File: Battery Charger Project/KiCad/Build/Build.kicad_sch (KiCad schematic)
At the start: 26 parts, among them J1 Screw_Terminal_01x03, J2 Screw_Terminal_01x02, J3 Screw_Terminal_01x03, J4 726386-2, J5 726386-2, J6 726386-2, U1 LAUNCHXL-F28379D, U2 TMCS1133C3A

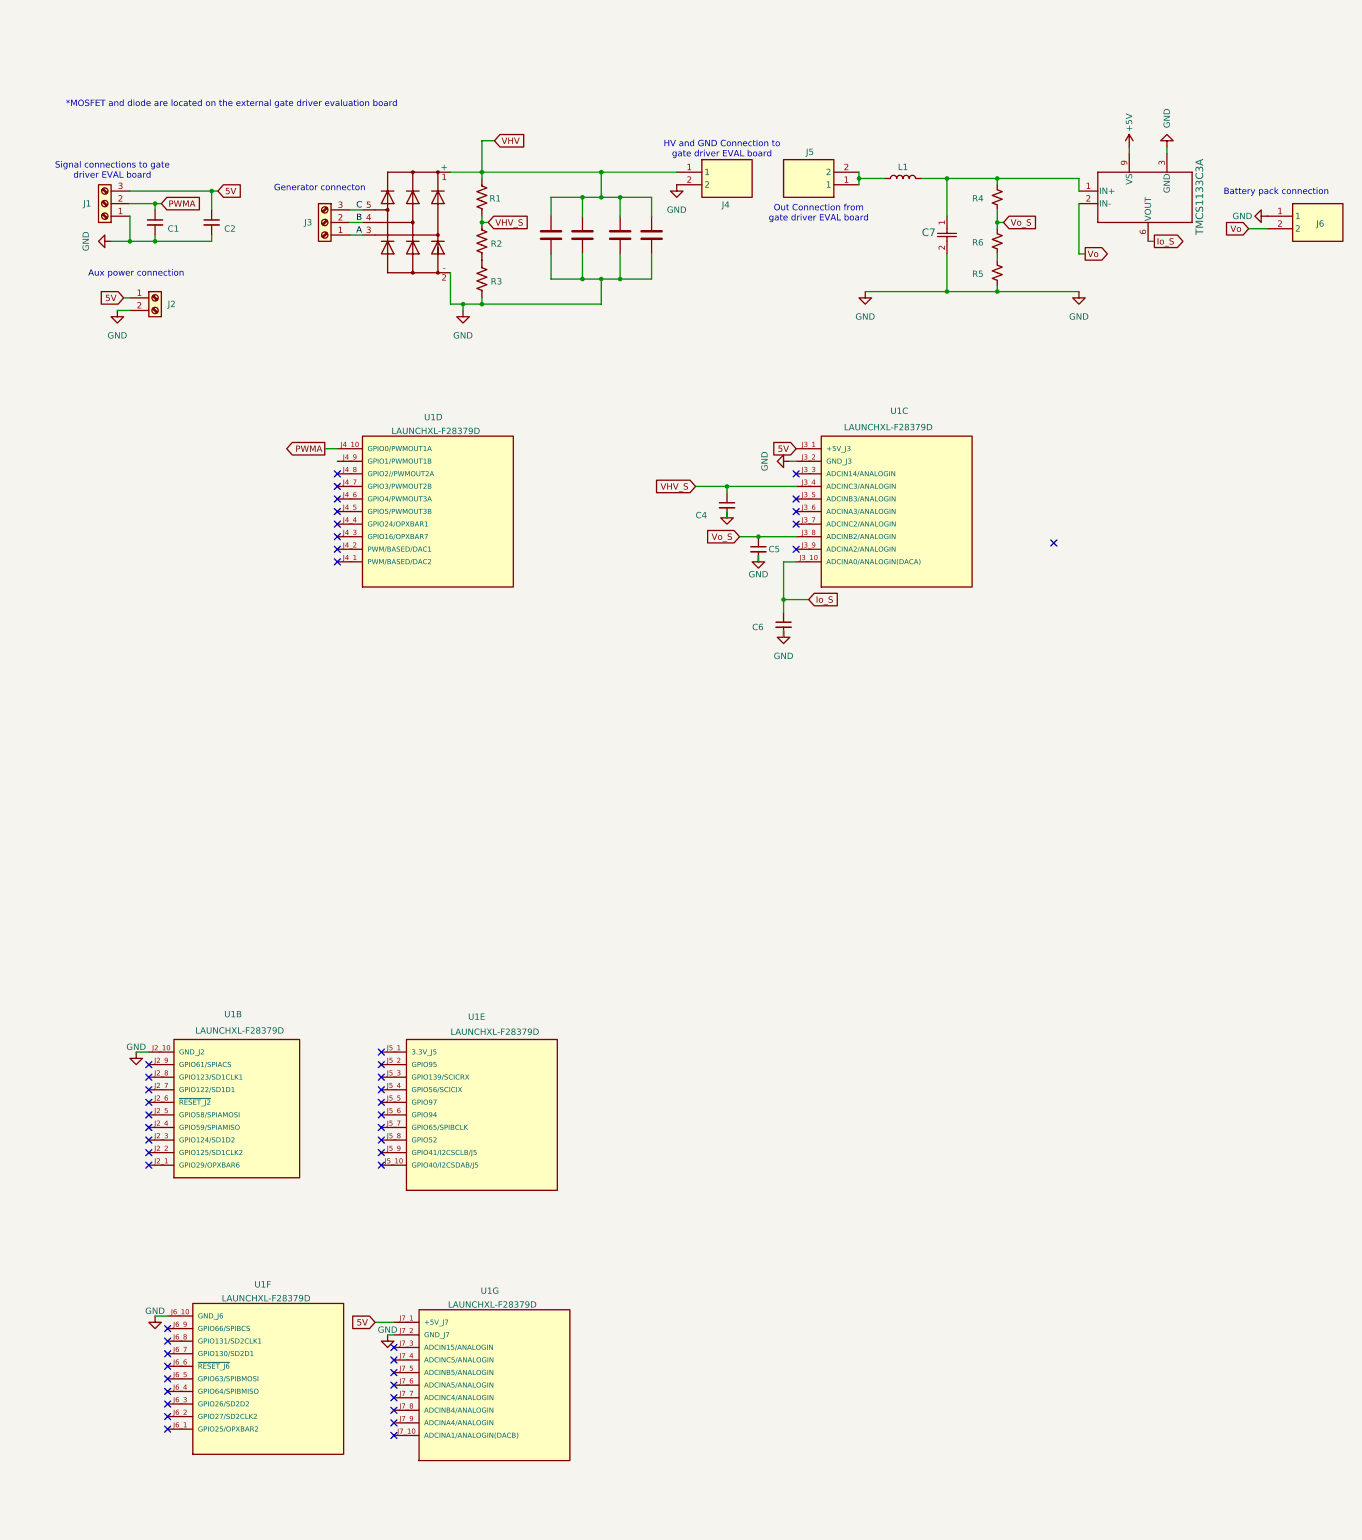
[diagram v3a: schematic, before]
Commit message: PCB updates
Dr. Mcintyre suggested using large pours for the high voltage and gnd planes. He also asked me to implement design constraints. The main concern is the distance between the high DC bus and gnd near the rectifier.
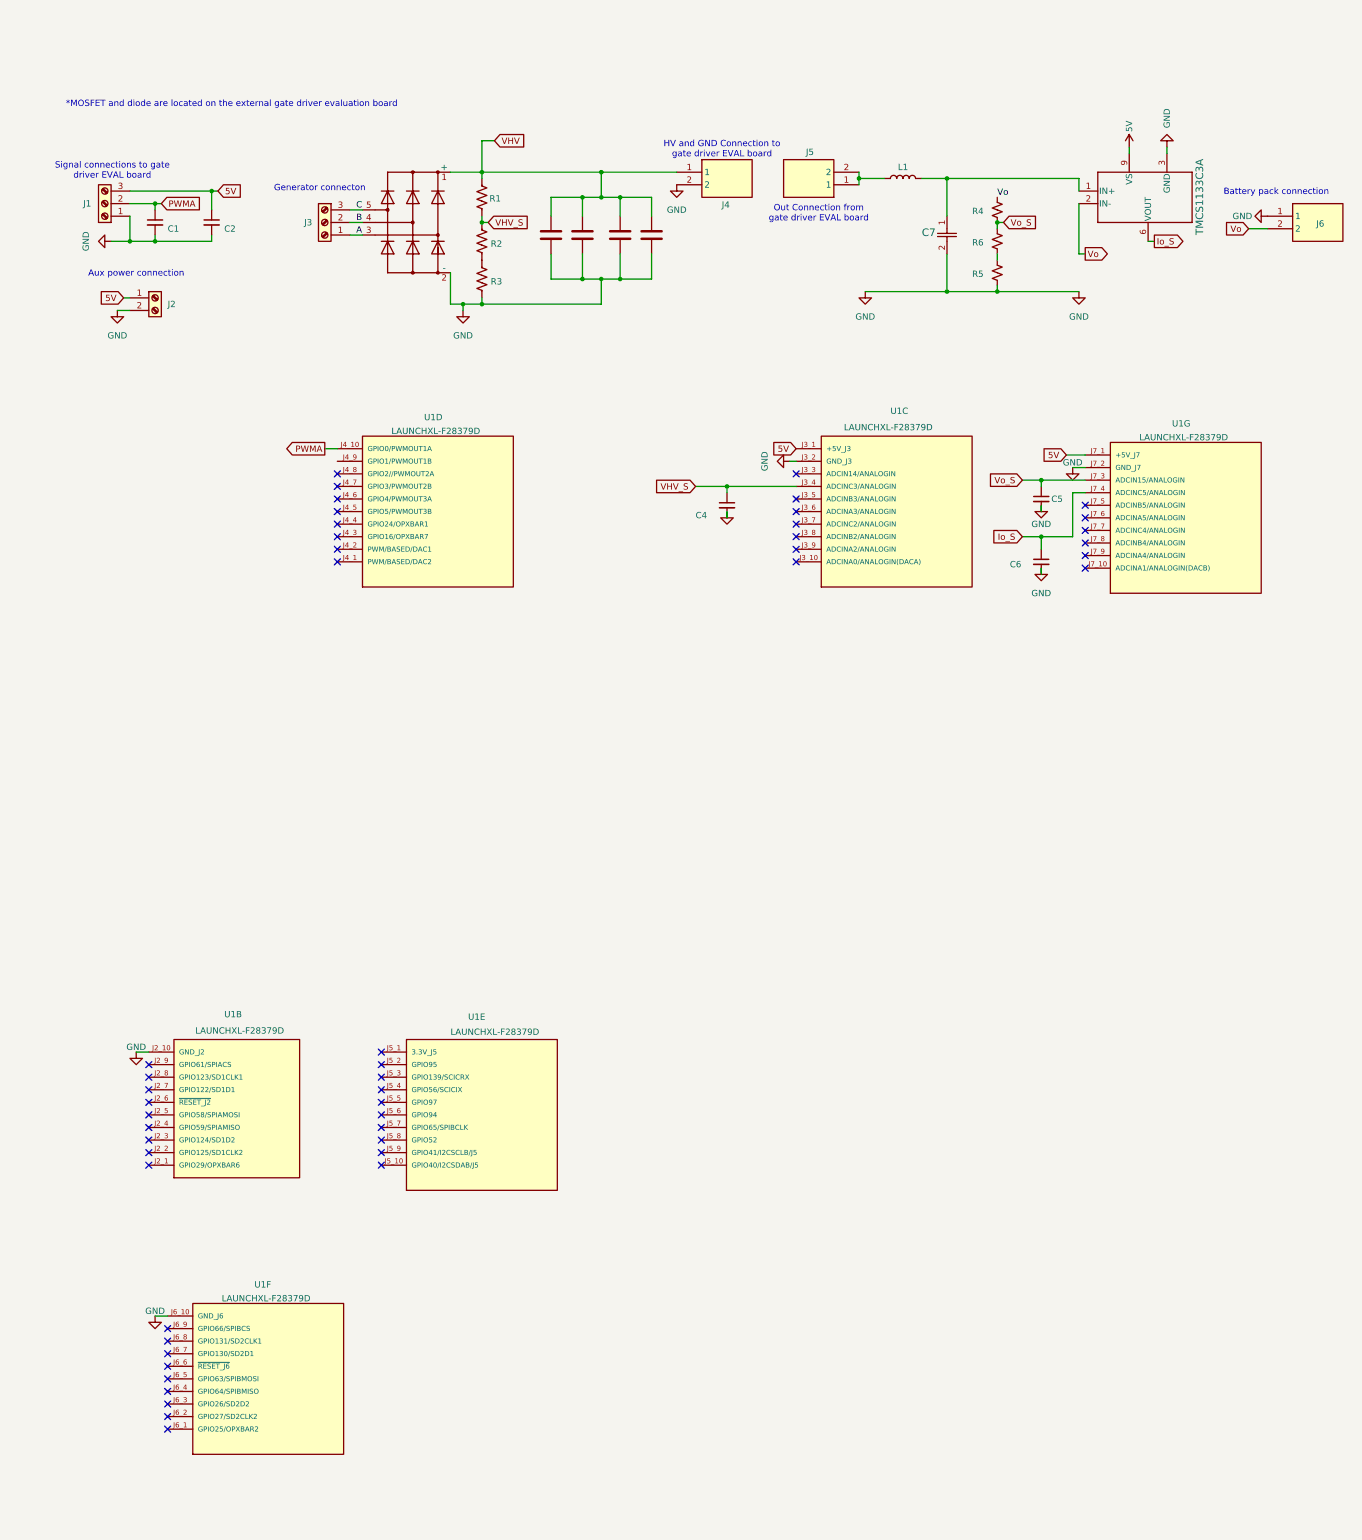
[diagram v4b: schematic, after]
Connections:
- net +5V is gone; now on net 5V: U2.9 (VS)
- net Io_S: now also U1.J7_4 (ADCINC5/ANALOGIN); no longer U1.J3_10 (ADCINA0/ANALOGIN(DACA))
- net Vo: now also R4.1
- net Vo_S: now also U1.J7_3 (ADCIN15/ANALOGIN); no longer U1.J3_8 (ADCINB2/ANALOGIN)
- net at C7.1, L1.2, U2.1 (IN+): no longer R4.1
- no-connect marks 50 -> 49
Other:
- moved on the sheet: C5, C6, R4, U1G

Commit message: PCB updates
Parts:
- added C11: C_Small, Capacitor_SMD:C_0805_2012Metric_Pad1.18x1.45mm_HandSolder, symbol Device:C_Small
- added unit 1 of U1
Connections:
- net 5V: no longer U1.J7_1 (+5V_J7), U2.9 (VS)
- net GND: now also C11.2
- net VHV_S: now also U1.J3_10 (ADCINA0/ANALOGIN(DACA)); no longer U1.J3_4 (ADCINC3/ANALOGIN)
- new net +3.3V: C11.1, U1.J1_1 (3.3V_J1), U2.10 (VS), U2.9 (VS)
- no-connect marks 49 -> 58
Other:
- moved on the sheet: C4, C5, C6, U1C, U1G

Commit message: PCB about done
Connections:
- net +3.3V: now also U2.8 (VOC)
- net GND: now also U2.4 (ALERT), U2.7 (OC)
- net Io_S: now also U1.J7_5 (ADCINB5/ANALOGIN); no longer U1.J7_4 (ADCINC5/ANALOGIN)
- net VHV_S: now also U1.J3_8 (ADCINB2/ANALOGIN); no longer U1.J3_10 (ADCINA0/ANALOGIN(DACA))
- net Vo_S: now also U1.J7_4 (ADCINC5/ANALOGIN); no longer U1.J7_3 (ADCIN15/ANALOGIN)
- no-connect marks 58 -> 61
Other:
- moved on the sheet: C11, C4, C5

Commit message: PCB complete
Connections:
- net Voh: now reaches C7.1, L1.2, U2.1 (IN+)
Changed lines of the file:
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@@
+	)
+	(junction
+		(at 224.79 54.61)
+		(diameter 0)
+		(color 0 0 0 0)
 	)
 	(junction
@@
 	(wire
 		(pts
+			(xy 223.52 52.07) (xy 224.79 54.61)
+		)
+		(stroke
+			(width 0)
+			(type default)
+		)
+	)
+	(wire
+		(pts
 			(xy 245.11 45.72) (xy 245.11 44.45)
 		)
@@
 	(wire
 		(pts
-			(xy 200.66 54.61) (xy 227.33 54.61)
+			(xy 200.66 54.61) (xy 224.79 54.61)
 		)
 		(stroke
@@
 		(pts
 			(xy 40.64 59.69) (xy 40.64 60.96)
+		)
+		(stroke
+			(width 0)
+			(type default)
+		)
+	)
+	(wire
+		(pts
+			(xy 224.79 54.61) (xy 227.33 54.61)
 		)
 		(stroke
@@
 		(effects
 			(font
+				(size 1.27 1.27)
+			)
+			(justify left bottom)
+		)
+	)
+	(label "Voh"
+		(at 223.52 52.07 0)
+		(effects
+			(font

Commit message: PCB ORDERED
This push contains the PCB version and Gerber files that were ordered for the first prototype.
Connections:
- net +3.3V: now also C2.1, J1.3 (Pin_3), J2.1 (Pin_1)
- net 5V: no longer C2.1, J1.3 (Pin_3), J2.1 (Pin_1)
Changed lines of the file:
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@@
 		)
 	)
-	(global_label "5V"
-		(shape input)
-		(at 34.29 78.74 180)
-		(fields_autoplaced yes)
-		(effects
-			(font
-				(size 1.27 1.27)
-			)
-			(justify right)
-		)
-		(property "Intersheetrefs" "${INTERSHEET_REFS}"
-			(at 29.0067 78.74 0)
-			(hide yes)
-			(show_name no)
-			(do_not_autoplace no)
-			(effects
-				(font
-					(size 1.27 1.27)
-				)
-				(justify right)
-			)
-		)
-	)
 	(global_label "PWMA"
 		(shape output)
@@
 		)
 	)
-	(global_label "5V"
-		(shape input)
-		(at 53.34 57.15 0)
-		(fields_autoplaced yes)
-		(effects
-			(font
-				(size 1.27 1.27)
-			)
-			(justify left)
-		)
-		(property "Intersheetrefs" "${INTERSHEET_REFS}"
-			(at 58.6233 57.15 0)
-			(hide yes)
-			(show_name no)
-			(do_not_autoplace no)
-			(effects
-				(font
-					(size 1.27 1.27)
-				)
-				(justify left)
-			)
-		)
-	)
 	(global_label "PWMA"
 		(shape input)
@@
 	)
 	(symbol
+		(lib_id "power:+3.3V")
+		(at 90.17 284.48 90)
+		(unit 1)
+		(body_style 1)
+		(exclude_from_sim no)
+		(in_bom yes)
+		(on_board yes)
+		(in_pos_files yes)
+		(dnp no)
+		(fields_autoplaced yes)
+		(property "Reference" "#PWR020"
+			(at 93.98 284.48 0)
+			(hide yes)
+			(show_name no)
+			(do_not_autoplace no)
+			(effects
+				(font
+					(size 1.27 1.27)
+				)
+			)
+		)
+		(property "Value" "+3.3V"
+			(at 86.36 284.4799 90)
+			(show_name no)
+			(do_not_autoplace no)
+			(effects
+				(font
+					(size 1.27 1.27)
+				)
+				(justify left)
+			)
+		)
+		(property "Footprint" ""
+			(at 90.17 284.48 0)
+			(hide yes)
+			(show_name no)
+			(do_not_autoplace no)
+			(effects
+				(font
+					(size 1.27 1.27)
+				)
+			)
+		)
+		(property "Datasheet" ""
+			(at 90.17 284.48 0)
+			(hide yes)
+			(show_name no)
+			(do_not_autoplace no)
+			(effects
+				(font
+					(size 1.27 1.27)
+				)
+			)
+		)
+		(property "Description" "Power symbol creates a global label with name \"+3.3V\""
+			(at 90.17 284.48 0)
+			(hide yes)
+			(show_name no)
+			(do_not_autoplace no)
+			(effects
+				(font
+					(size 1.27 1.27)
+				)
+			)
+		)
+		(pin "1"
+		)
+		(instances
+			(project "Build"
+				(path "/e008d697-99dc-4867-8b55-c16283d519fc"
+					(reference "#PWR020")
+					(unit 1)
+				)
+			)
+		)
+	)
+	(symbol
 		(lib_id "power:GND")
 		(at 102.87 81.28 0)
@@
 	)
 	(symbol
+		(lib_id "power:+3.3V")
+		(at 34.29 78.74 90)
+		(unit 1)
+		(body_style 1)
+		(exclude_from_sim no)
+		(in_bom yes)
+		(on_board yes)
+		(in_pos_files yes)
+		(dnp no)
+		(fields_autoplaced yes)
+		(property "Reference" "#PWR021"
+			(at 38.1 78.74 0)
+			(hide yes)
+			(show_name no)
+			(do_not_autoplace no)
+			(effects
+				(font
+					(size 1.27 1.27)
+				)
+			)
+		)
+		(property "Value" "+3.3V"
+			(at 30.48 78.7399 90)
+			(show_name no)
+			(do_not_autoplace no)
+			(effects
+				(font
+					(size 1.27 1.27)
+				)
+				(justify left)
+			)
+		)
+		(property "Footprint" ""
+			(at 34.29 78.74 0)
+			(hide yes)
+			(show_name no)
+			(do_not_autoplace no)
+			(effects
+				(font
+					(size 1.27 1.27)
+				)
+			)
+		)
+		(property "Datasheet" ""
+			(at 34.29 78.74 0)
+			(hide yes)
+			(show_name no)
+			(do_not_autoplace no)
+			(effects
+				(font
+					(size 1.27 1.27)
+				)
+			)
+		)
+		(property "Description" "Power symbol creates a global label with name \"+3.3V\""
+			(at 34.29 78.74 0)
+			(hide yes)
+			(show_name no)
+			(do_not_autoplace no)
+			(effects
+				(font
+					(size 1.27 1.27)
+				)
+			)
+		)
+		(pin "1"
+		)
+		(instances
+			(project "Build"
+				(path "/e008d697-99dc-4867-8b55-c16283d519fc"
+					(reference "#PWR021")
+					(unit 1)
+				)
+			)
+		)
+	)
+	(symbol
 		(lib_id "Connector:Screw_Terminal_01x03")
 		(at 30.48 59.69 180)
@@
 	)
 	(symbol
+		(lib_id "power:+3.3V")
+		(at 53.34 57.15 270)
+		(unit 1)
+		(body_style 1)
+		(exclude_from_sim no)
+		(in_bom yes)
+		(on_board yes)
+		(in_pos_files yes)
+		(dnp no)
+		(fields_autoplaced yes)
+		(property "Reference" "#PWR022"
+			(at 49.53 57.15 0)
+			(hide yes)
+			(show_name no)
+			(do_not_autoplace no)
+			(effects
+				(font
+					(size 1.27 1.27)
+				)
+			)
+		)
+		(property "Value" "+3.3V"
+			(at 57.15 57.1499 90)
+			(show_name no)
+			(do_not_autoplace no)
+			(effects
+				(font
+					(size 1.27 1.27)
+				)
+				(justify left)
+			)
+		)
+		(property "Footprint" ""
+			(at 53.34 57.15 0)
+			(hide yes)
+			(show_name no)
+			(do_not_autoplace no)
+			(effects
+				(font
+					(size 1.27 1.27)
+				)
+			)
+		)
+		(property "Datasheet" ""
+			(at 53.34 57.15 0)
+			(hide yes)
+			(show_name no)
+			(do_not_autoplace no)
+			(effects
+				(font
+					(size 1.27 1.27)
+				)
+			)
+		)
+		(property "Description" "Power symbol creates a global label with name \"+3.3V\""
+			(at 53.34 57.15 0)
+			(hide yes)
+			(show_name no)
+			(do_not_autoplace no)
+			(effects
+				(font
+					(size 1.27 1.27)
+				)
+			)
+		)
+		(pin "1"
+		)
+		(instances
+			(project "Build"
+				(path "/e008d697-99dc-4867-8b55-c16283d519fc"
+					(reference "#PWR022")
+					(unit 1)
+				)
+			)
+		)
+	)
+	(symbol
 		(lib_id "mouseric:726386-2")
 		(at 265.43 62.23 0)
@@
 					(unit 1)
 				)
-			)
-		)
-	)
-	(symbol
-		(lib_id "power:+3.3V")
-		(at 90.17 284.48 90)
-		(unit 1)
-		(body_style 1)
-		(exclude_from_sim no)
-		(in_bom yes)
-		(on_board yes)
-		(in_pos_files yes)
-		(dnp no)
-		(fields_autoplaced yes)
-		(property "Reference" "#PWR017"
-			(at 93.98 284.48 0)
-			(hide yes)
-			(show_name no)
-			(do_not_autoplace no)
-			(effects
-				(font
-					(size 1.27 1.27)
-				)
-			)
-		)
-		(property "Value" "+3.3V"
-			(at 86.36 284.4799 90)
-			(show_name no)
-			(do_not_autoplace no)
-			(effects
-				(font
-					(size 1.27 1.27)
-				)
-				(justify left)
-			)
-		)
-		(property "Footprint" ""
-			(at 90.17 284.48 0)
-			(hide yes)
-			(show_name no)
-			(do_not_autoplace no)
-			(effects
-				(font
-					(size 1.27 1.27)
-				)
-			)
-		)
-		(property "Datasheet" ""
-			(at 90.17 284.48 0)
-			(hide yes)
-			(show_name no)
-			(do_not_autoplace no)
-			(effects
-				(font
-					(size 1.27 1.27)
-				)
-			)
-		)
-		(property "Description" "Power symbol creates a global label with name \"+3.3V\""
-			(at 90.17 284.48 0)
-			(hide yes)
-			(show_name no)
-			(do_not_autoplace no)
-			(effects
-				(font
-					(size 1.27 1.27)
-				)
-			)
-		)
-		(pin "1"
-		)
-		(instances
-			(project "Build"
-				(path "/e008d697-99dc-4867-8b55-c16283d519fc"
-					(reference "#PWR017")
-					(unit 1)
-				)
